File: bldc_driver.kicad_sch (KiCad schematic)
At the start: 19 parts, among them Q1 DI030N10PT-AQ, Q2 DI030N10PT-AQ, Q3 DI030N10PT-AQ, Q4 DI030N10PT-AQ, Q5 DI030N10PT-AQ, Q6 DI030N10PT-AQ, U1 STM32F318K8Ux, U2 DRV8311S, U4 MIC5504-1.8YM5, Y1 Crystal_GND24

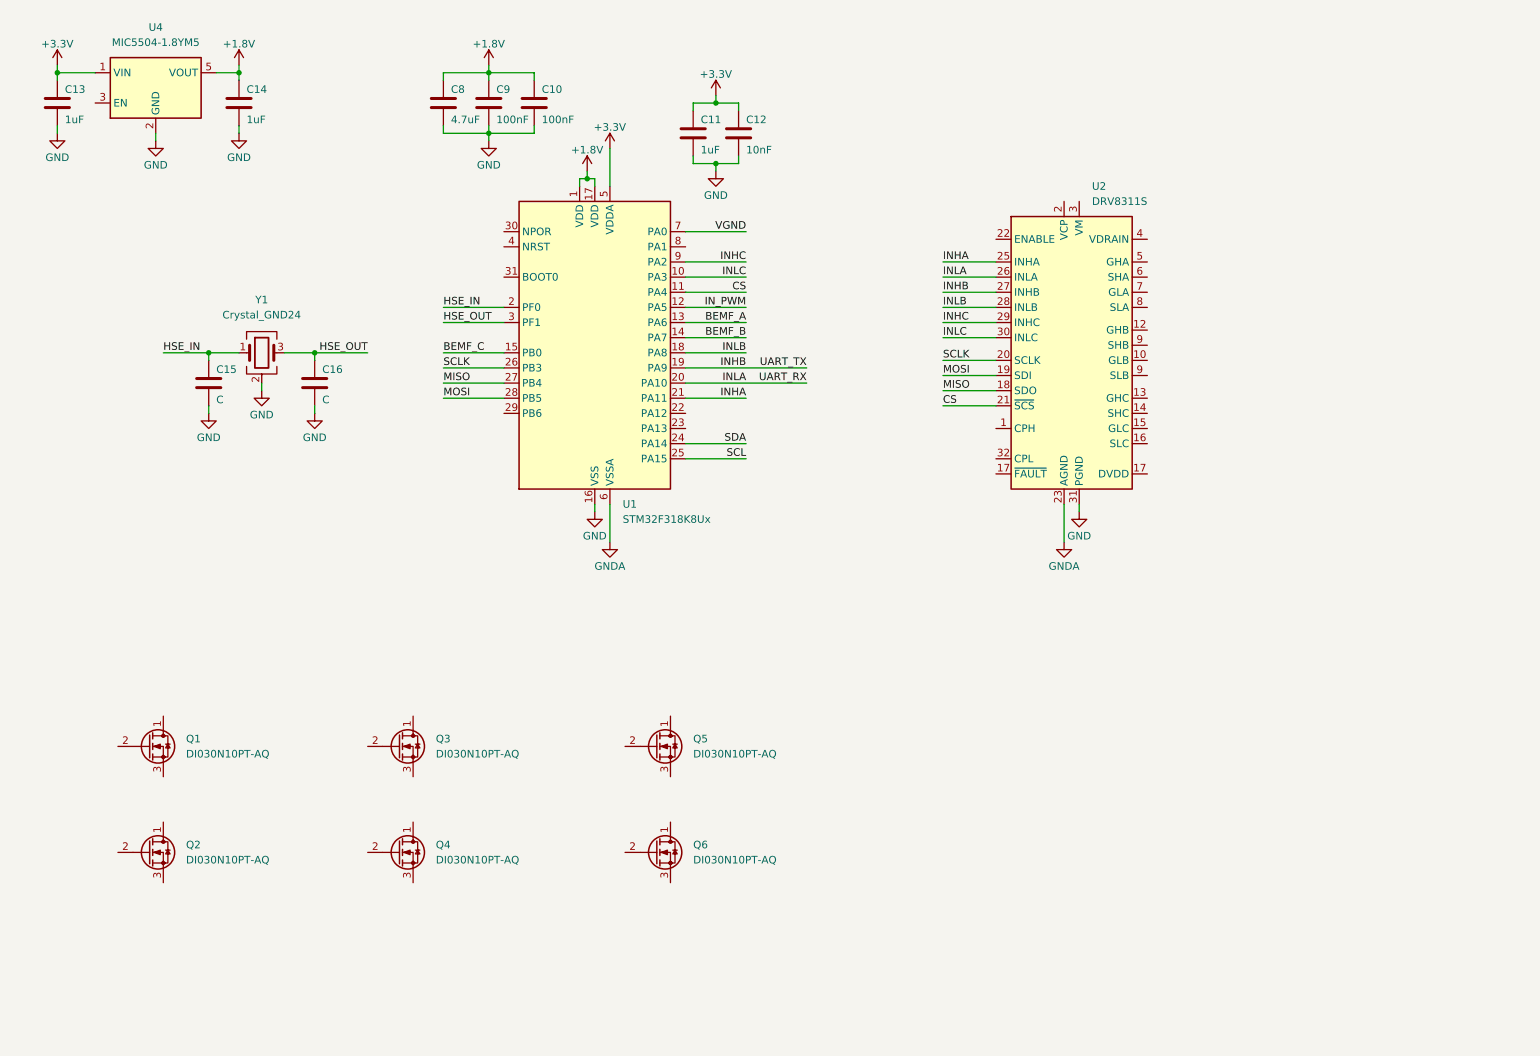
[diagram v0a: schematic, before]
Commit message: started wiring gate driver
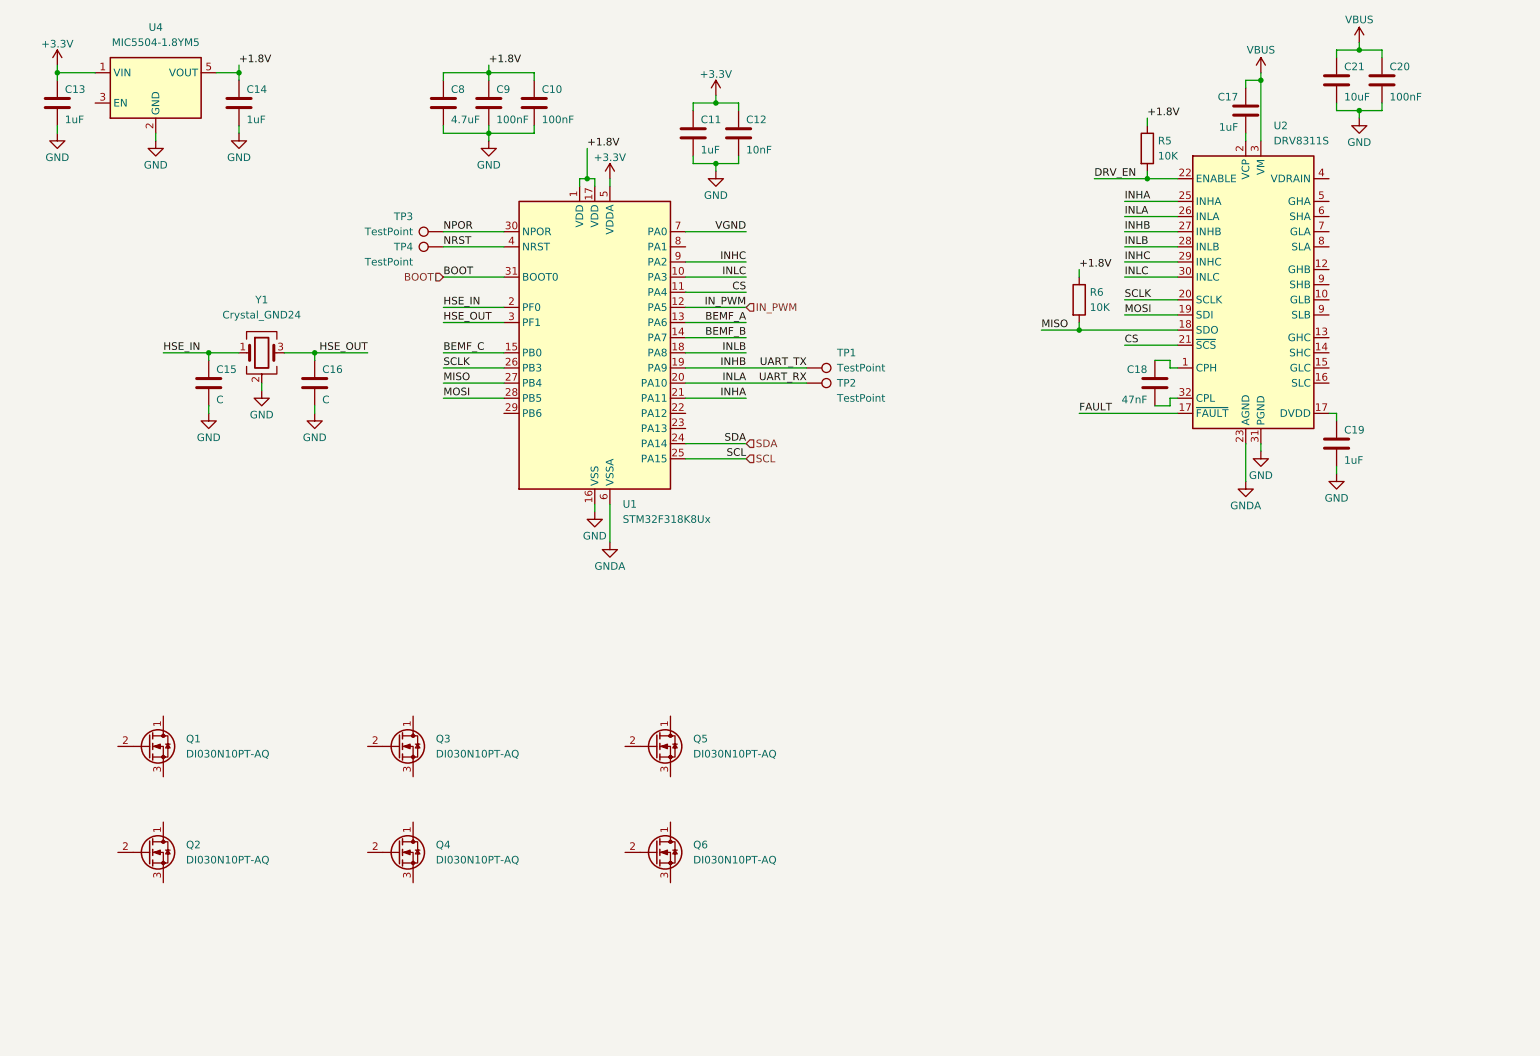
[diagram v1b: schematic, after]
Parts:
- added C17, C19: 1uF, Capacitor_SMD:C_0402_1005Metric, symbol Device:C
- added C18: 47nF, Capacitor_SMD:C_0402_1005Metric, symbol Device:C
- added C20: 100nF, Capacitor_SMD:C_0402_1005Metric, symbol Device:C
- added C21: 10uF, Capacitor_SMD:C_0402_1005Metric, symbol Device:C
- added R5, R6: 10K, symbol Device:R
- added TP1, TP2, TP3, TP4: TestPoint, TestPoint:TestPoint_Pad_D2.0mm, symbol Connector:TestPoint
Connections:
- net +1.8V: now also R5.1, R6.1
- net GND: now also C19.2, C20.2, C21.2
- net INHB: now also TP1.1
- net INLA: now also TP2.1
- net MISO: now also R6.2
- net at U2.1 (CPH): now also C18.1
- net FAULT: now reaches U2.17 (DVDD)
- net at U2.2 (VCP): now also C17.2
- net DRV_EN: now reaches U2.22 (ENABLE)
- net DRV_EN: now also R5.2
- net VBUS: now reaches U2.3 (VM)
- net VBUS: now also C17.1, C20.1, C21.1
- net at U2.32 (CPL): now also C18.2
- net NPOR: now reaches U1.30 (NPOR)
- net NPOR: now also TP3.1
- net BOOT: now reaches U1.31 (BOOT0)
- net NRST: now reaches U1.4 (NRST)
- net NRST: now also TP4.1
- new net: C19.1, U2.17 (DVDD)
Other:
- moved on the sheet: U2

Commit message: finished driver circuit
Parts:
- removed U2: DRV8311S, Package_DFN_QFN:WQFN-32-1EP_5x5mm_P0.5mm_EP3.1x3.1mm, symbol Multi-ESC:DRV8311S
- added C22: 10nF, Capacitor_SMD:C_0402_1005Metric, symbol Device:C
- added D1: SMAJ40CA, Diode_SMD:D_SMA, symbol Diode:SMAJ40CA
- added J1, J2, J3: Conn_01x01, symbol Connector_Generic:Conn_01x01
- added Q7: Q_PMOS_DGS, Package_DIP:DIP-24_W7.62mm, symbol Transistor_FET:Q_PMOS_DGS
- added R10, R12, R14: 18K, symbol Device:R
- added R11, R13, R9: 200K, symbol Device:R
- added R15, R16, R17: 200K, Package_DFN_QFN:WQFN-32-1EP_5x5mm_P0.5mm_EP3.1x3.1mm, symbol Device:R
- added R7: 1K, symbol Device:R
- added R8: 10K, symbol Device:R
- added U2: DRV8320SR, Package_DFN_QFN:WQFN-32-1EP_5x5mm_P0.5mm_EP3.1x3.1mm, symbol Multi-ESC:DRV8320SR
- C15, C16: value C -> 10pF
- Y1: value Crystal_GND24 -> 8MHz; MPN (none) -> STDCRA3-8M
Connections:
- net +1.8V: now also R8.1
- net BEMF_A: now also R10.1, R11.2, R12.1, R13.2, R14.1, R15.1, R9.2
- net BEMF_B: now also R16.1
- net BEMF_C: now also R17.1
- net CS: now also U2.21 (~{SCS})
- net DRV_EN: now also U2.22 (ENABLE)
- net FAULT: now also R8.2, U2.17 (DVDD)
- net GND: now also Q2.3 (S), Q4.3 (S), Q6.3 (S), C22.2, D1.1 (A1), R10.2, R12.2, R14.2, R7.2, U2.16 (SLC), U2.31 (PGND), U2.33 (PGND), U2.8 (SLA), U2.9 (SLB)
- net GNDA: now also U2.23 (AGND)
- net INHA: now also U2.25 (INHA)
- net INHB: now also U2.27 (INHB)
- net INHC: now also U2.29 (INHC)
- net INLA: now also U2.26 (INLA)
- net INLB: now also U2.28 (INLB)
- net INLC: now also U2.30 (INLC)
- net MISO: now also U2.18 (SDO)
- net MOSI: now also U2.19 (SDI)
- net SCLK: now also U2.20 (SCLK)
- net VBUS: now also D1.2 (A2), Q7.1 (D); no longer C17.1, C20.1, C21.1
- net VGND: now also C22.1, R16.2
- net VM: now reaches Q1.1 (D)
- net VM: now also C17.1, C20.1, C21.1, Q3.1 (D), Q5.1 (D), Q7.3 (S), U2.3 (VM), U2.4 (VDRAIN)
- net GHA: now reaches Q1.2 (G)
- net GHA: now also U2.5 (GHA)
- net SHA: now reaches Q1.3 (S)
- net SHA: now also Q2.1 (D), J1.1 (Pin_1), R9.1, U2.6 (SHA)
- net GHB: now reaches Q3.2 (G)
- net GHB: now also U2.12 (GHB)
- net SHB: now reaches Q3.3 (S)
- net SHB: now also Q4.1 (D), J2.1 (Pin_1), R11.1, U2.9 (SLB)
- net at C19.1: now also U2.17 (DVDD)
- net at C18.1: now also U2.1 (CPH)
- net at C17.2: now also U2.2 (VCP)
- net at C18.2: now also U2.32 (CPL)
- net GLA: now reaches Q2.2 (G)
- net GLA: now also U2.7 (GLA)
- net GLB: now reaches Q4.2 (G)
- net GLB: now also U2.10 (GLB)
- net SHC: now reaches Q6.1 (D)
- net SHC: now also Q5.3 (S), J3.1 (Pin_1), R13.1, U2.14 (SHC)
- net GLC: now reaches Q6.2 (G)
- net GLC: now also U2.15 (GLC)
- net GHC: now reaches Q5.2 (G)
- net GHC: now also U2.13 (GHC)
- new net: R15.2, R17.2
- new net: Q7.2 (G), R7.1
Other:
- moved on the sheet: C17, C18, C19, C20, C21, Q1, Q2, R5, R6

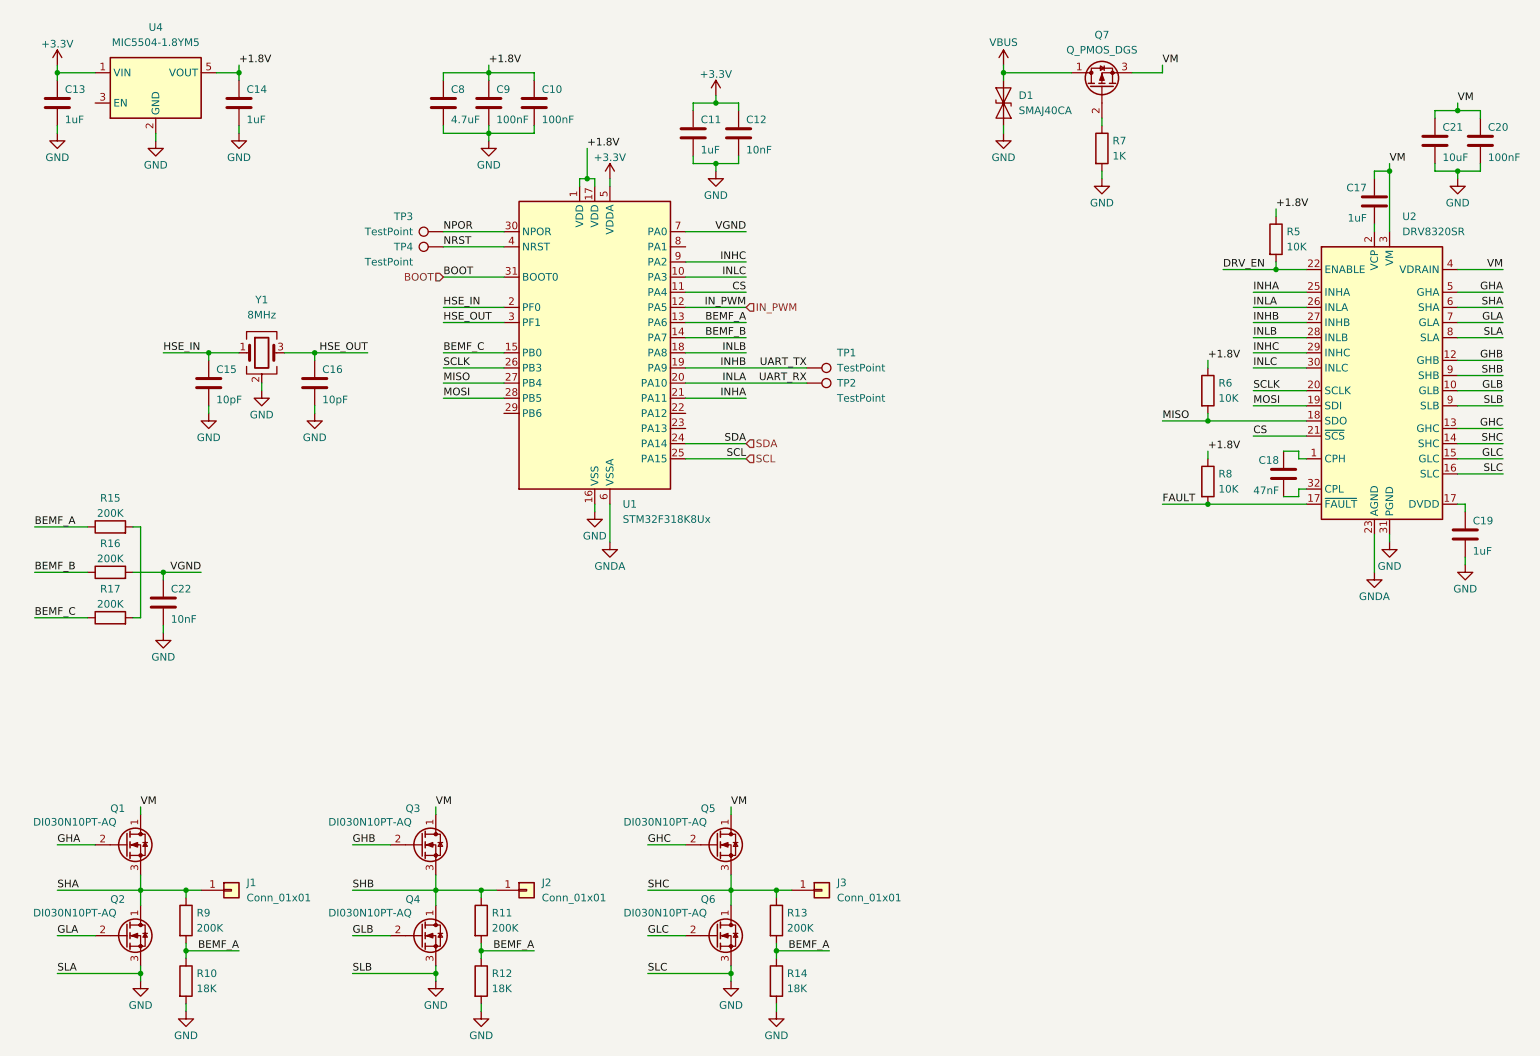
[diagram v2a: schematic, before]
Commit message: added bulk capacitance
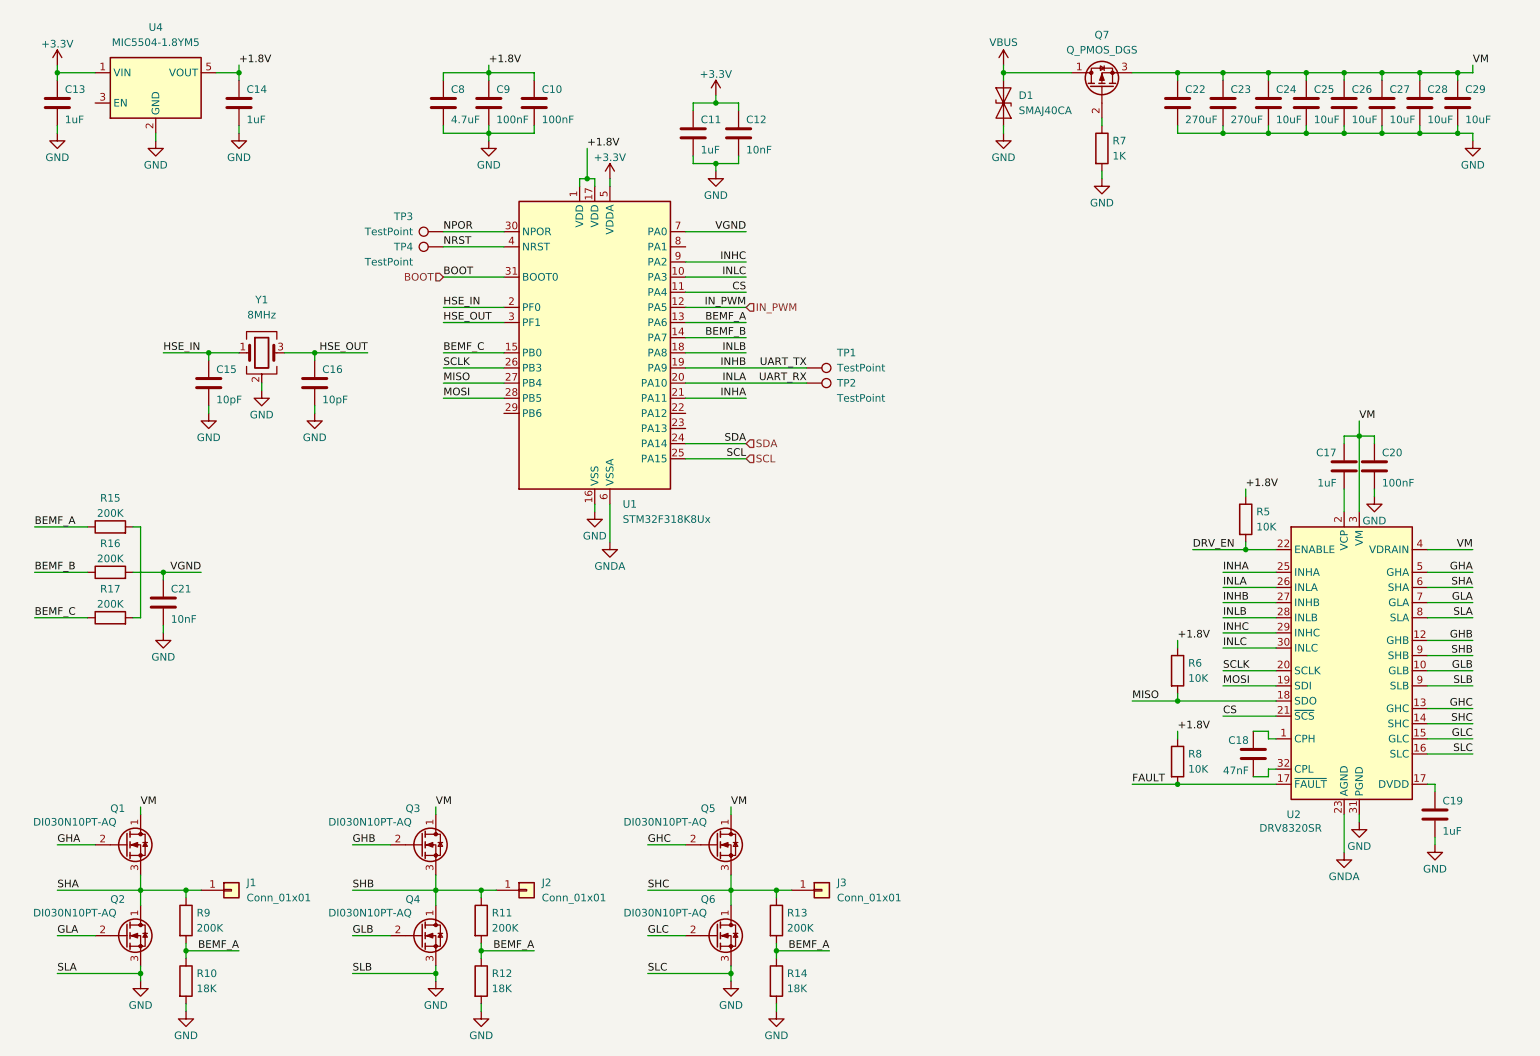
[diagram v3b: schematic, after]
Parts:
- removed C21: 10uF, Capacitor_SMD:C_0402_1005Metric, symbol Device:C
- added C22, C23: 270uF, Capacitor_SMD:C_0402_1005Metric, symbol Device:C
- added C24, C25, C26, C27, C28, C29: 10uF, Capacitor_SMD:C_0402_1005Metric, symbol Device:C
- renumbered C22 to C21
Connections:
- net GND: now also C22.2, C23.2, C24.2, C25.2, C26.2, C27.2, C28.2, C29.2
- net VM: now also C22.1, C23.1, C24.1, C25.1, C26.1, C27.1, C28.1, C29.1
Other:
- moved on the sheet: C17, C18, C19, C20, R5, R6, R8, U2

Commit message: adding analog protection
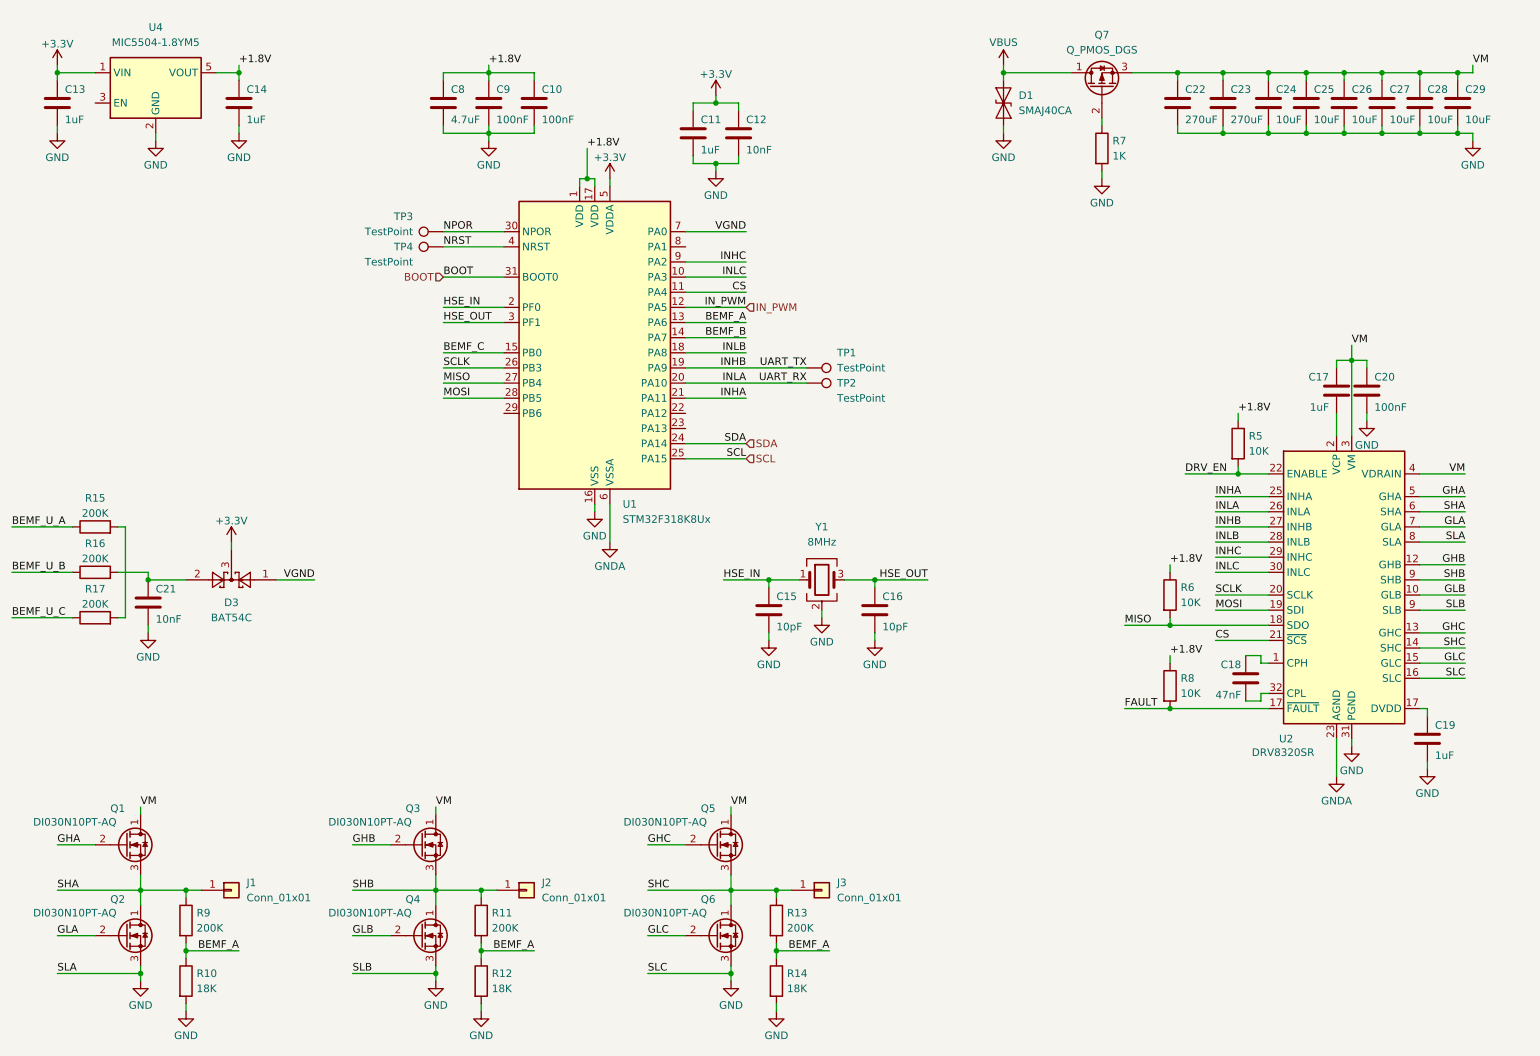
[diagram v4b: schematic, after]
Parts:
- added D3: BAT54C, Package_TO_SOT_SMD:SOT-23, symbol Diode:BAT54C
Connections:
- net +3.3V: now also D3.3
- net BEMF_A: no longer R15.1
- net BEMF_B: no longer R16.1
- net BEMF_C: no longer R17.1
- net VGND: now also D3.1; no longer C21.1, R16.2
- new net: C21.1, D3.2, R16.2
- new net BEMF_U_A: R15.1
- new net BEMF_U_B: R16.1
- new net BEMF_U_C: R17.1
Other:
- moved on the sheet: C15, C16, C17, C18, C19, C20, C21, R15, R16, R17, R5, R6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

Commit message: completed analog protetion
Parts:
- added D4, D5, D6: BAT54C, Package_TO_SOT_SMD:SOT-23, symbol Diode:BAT54C
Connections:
- net +3.3V: now also D4.3, D5.3, D6.3
- net BEMF_A: now also D4.1
- net BEMF_B: now also D5.1
- net BEMF_C: now also D6.1
- net BEMF_U_A: now also D4.2
- net BEMF_U_B: now also D5.2
- net BEMF_U_C: now also D6.2
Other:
- moved on the sheet: C21, D3, R15, R16, R17

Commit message: started pcb layout
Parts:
- C22, C23: footprint Capacitor_SMD:C_0402_1005Metric -> Capacitor_SMD:C_Elec_10x10.2
- J1, J2, J3: footprint (none) -> Connector_Wire:SolderWire-4sqmm_1x01_D3mm_OD6mm
- Q1, Q2, Q3, Q4, Q5, Q6: footprint (none) -> Diode_SMD:D_QFN_3.3x3.3mm_P0.65mm
- Q7: footprint Package_DIP:DIP-24_W7.62mm -> Package_SO:PowerPAK_SO-8L_Single
- R10, R11, R12, R13, R14, R5, R6, R7, R8, R9: footprint (none) -> Resistor_SMD:R_0402_1005Metric
